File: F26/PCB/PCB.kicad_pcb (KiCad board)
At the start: 2 copper layers, 6 parts, among them J3 B2B-XH-A, J4 B3B-XH-A, U4 815, U6 SC0194_9_

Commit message: Unfinished PCB Design
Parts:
- added SW1: SW_Nidec_CAS-120A1, Button_Switch_SMD:Nidec_Copal_CAS-120A, F.Cu at (73.5, 97.8)
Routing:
- net Net-(U1-A5): track 108.3 -> 166.6 mm
- net Net-(U4-~{OE}-PadOE_1): track 0.00 -> 58.3 mm
- net Net-(U1-A4): track 71.9 -> 130.2 mm
- net Net-(SW1-B): track 129.0 -> 180.4 mm

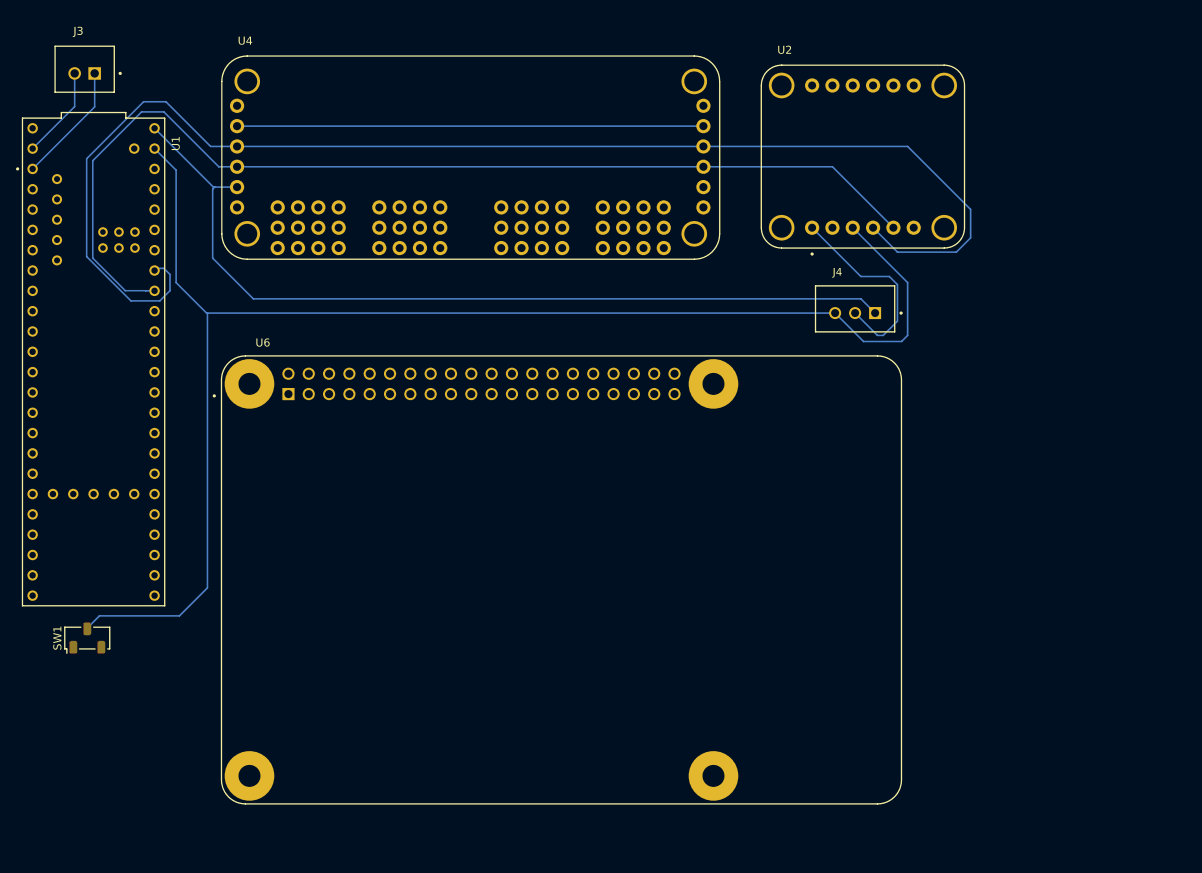
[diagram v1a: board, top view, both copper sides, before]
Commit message: Worded on PCB and teensy implementation
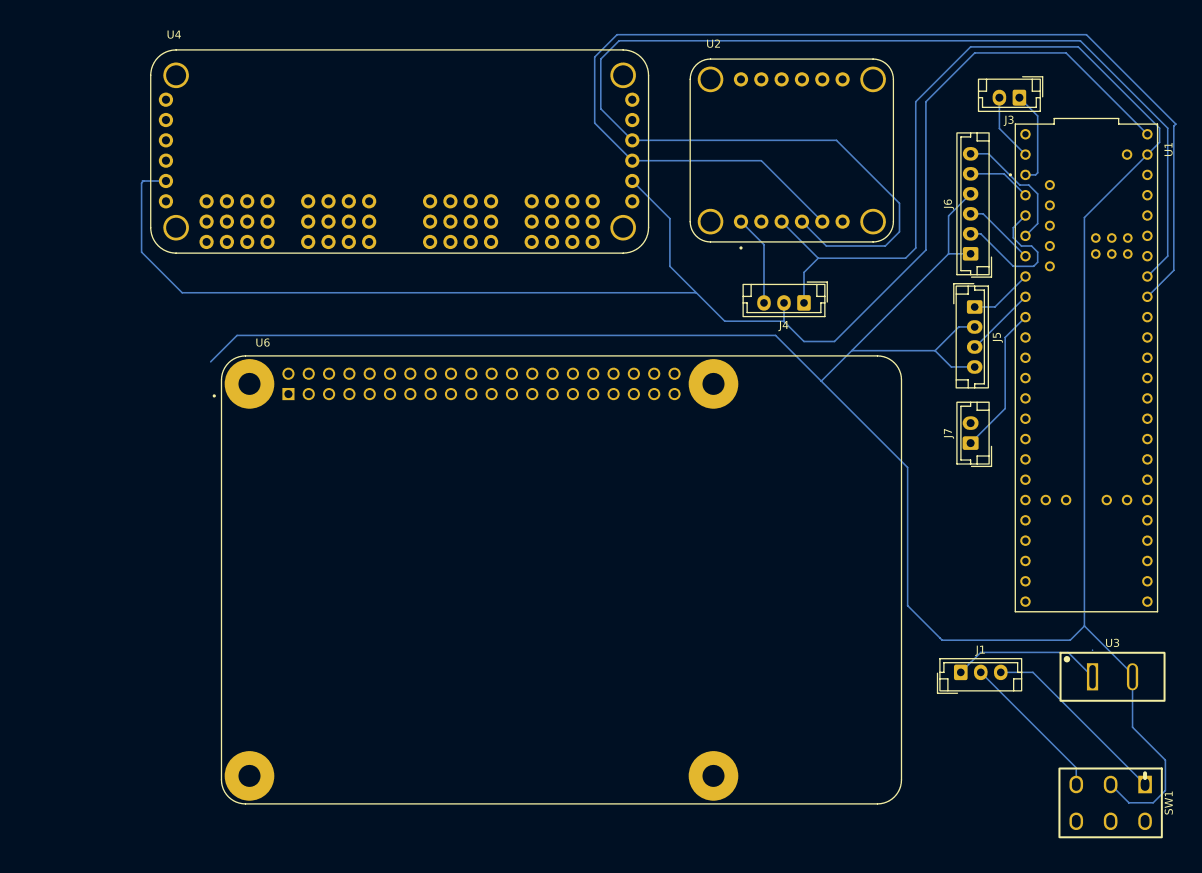
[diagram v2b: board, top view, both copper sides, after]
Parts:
- added J1: B3B-XH-A, Connector_JST:JST_EH_B3B-EH-A_1x03_P2.50mm_Vertical, F.Cu at (182.7, 102.1)
- added J5: Conn_01x04, Connector_JST:JST_EH_B4B-EH-A_1x04_P2.50mm_Vertical, F.Cu at (184.4, 56.4)
- added J6: Conn_01x06, Connector_JST:JST_EH_B6B-EH-A_1x06_P2.50mm_Vertical, F.Cu at (183.9, 49.7)
- added J7: Conn_01x02, Connector_JST:JST_EH_B2B-EH-A_1x02_P2.50mm_Vertical, F.Cu at (183.9, 73.4)
- added U3: ~, Button:Switch_2Pin_5mm_ParallelBlades, F.Cu at (199.1, 102.6)
- J3: footprint JST:JST -> Connector_JST:JST_EH_B2B-EH-A_1x02_P2.50mm_Vertical
- J4: footprint JST3:JST3 -> Connector_JST:JST_EH_B3B-EH-A_1x03_P2.50mm_Vertical
- SW1: footprint Button_Switch_SMD:Nidec_Copal_CAS-120A -> Switch:Mini_Toggle_DPDT_4.3x4.6mm
- moved SW1 129.6 mm to (201.4, 118.4), turned to -90 degrees
- moved U1 124.1 mm to (198.4, 64.0)
- moved J3 116.9 mm to (190.0, 30.2), turned to 180 degrees
- moved U4 8.92 mm to (112.5, 37.0)
- moved U2 8.92 mm to (161.5, 36.8)
- moved J4 6.43 mm to (163.1, 55.9), turned to 180 degrees
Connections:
- J4 pad 1: VCC -> Net-(J5-Pin_2)
- J4 pad 2: Net-(U2-VIN) -> VCC
- J4 pad 3: Net-(SW1-B) -> Net-(U2-VIN)
- SW1 pad 2: Net-(SW1-B) -> Net-(J5-Pin_2)
- U1 pad 2: unconnected-(U1-OUT2-Pad2) -> Net-(J6-Pin_5)
- U1 pad 3: unconnected-(U1-LRCLK2-Pad3) -> Net-(J6-Pin_2)
- U1 pad 4: unconnected-(U1-BCLK2-Pad4) -> Net-(J6-Pin_6)
- U1 pad 5: unconnected-(U1-IN2-Pad5) -> Net-(J6-Pin_3)
- U1 pad 6: unconnected-(U1-OUT1D-Pad6) -> Net-(J5-Pin_1)
- U1 pad 7: unconnected-(U1-OUT1A-Pad7) -> Net-(J5-Pin_3)
- U1 pad 8: unconnected-(U1-IN1-Pad8) -> Net-(J7-Pin_1)
- U1 pad GND: Net-(SW1-B) -> Net-(J5-Pin_2)
- U2 pad 3: Net-(SW1-B) -> Net-(J5-Pin_2)
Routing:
- net Net-(J5-Pin_2): track 0.00 -> 374.2 mm
- net Net-(SW1-B): track 180.4 -> 0.00 mm
- net VCC: track 108.0 -> 191.9 mm
- net Net-(U4-~{OE}-PadOE_1): track 58.3 -> 0.00 mm
- net Net-(SW1-C): track 0.00 -> 23.8 mm
- net Net-(SW1-A): track 0.00 -> 19.0 mm
- net Net-(J1-Pad1): track 0.00 -> 18.8 mm
- net Net-(J6-Pin_2): track 0.00 -> 18.8 mm
- net Net-(J7-Pin_1): track 0.00 -> 18.6 mm
- net Net-(J6-Pin_6): track 0.00 -> 16.3 mm
- net Net-(U2-VIN): track 25.4 -> 11.9 mm
- net Net-(U1-A4): track 130.2 -> 143.3 mm
- net Net-(J6-Pin_3): track 0.00 -> 9.05 mm
- net Net-(J5-Pin_3): track 0.00 -> 8.95 mm
- net Net-(J6-Pin_5): track 0.00 -> 7.96 mm
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
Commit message: PCB updates and Made wiring diagram
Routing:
- net Net-(J5-Pin_2): track 374.2 -> 294.1 mm
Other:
- board outline added: 134.4 x 105.1 mm

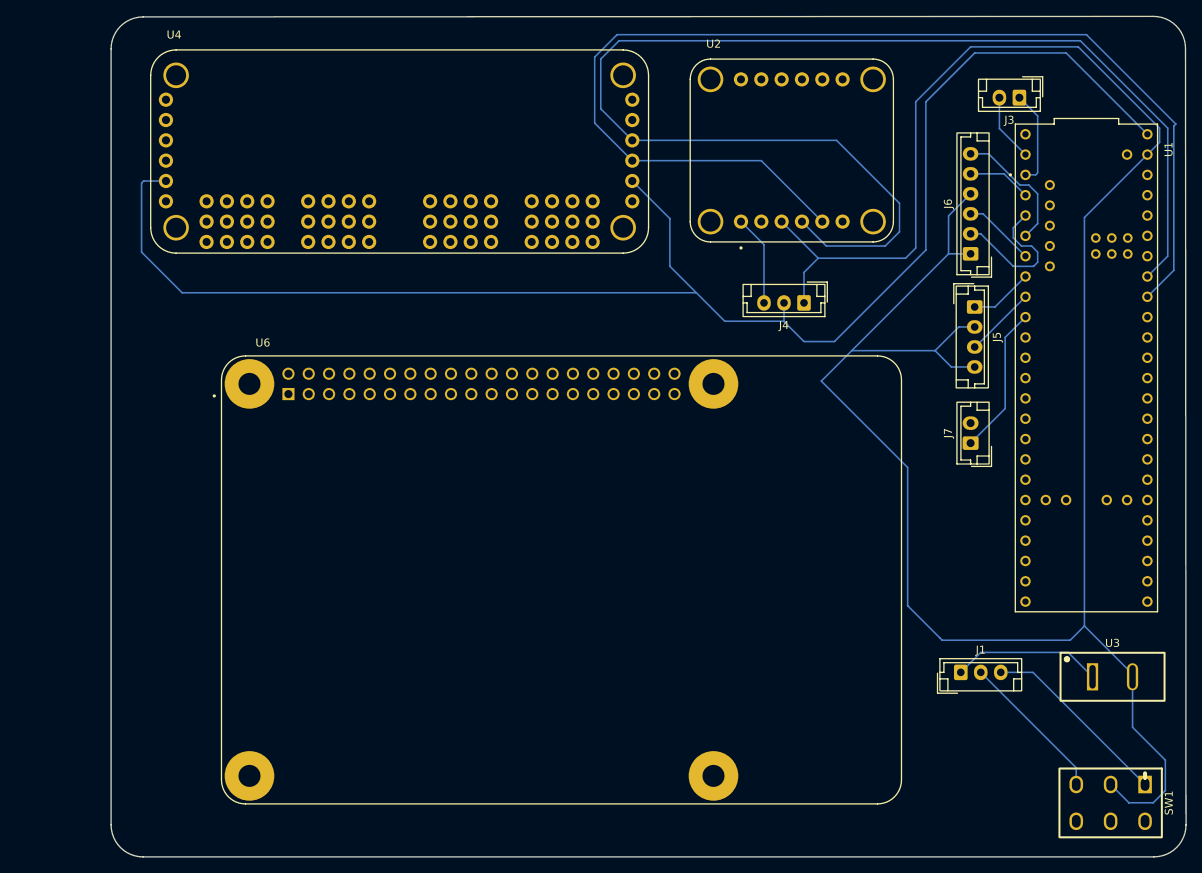
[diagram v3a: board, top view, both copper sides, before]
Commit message: Revert "PCB updates and Made wiring diagram"
This reverts commit 1d9744c909245b32a5317365d398eff2a277c9bc.
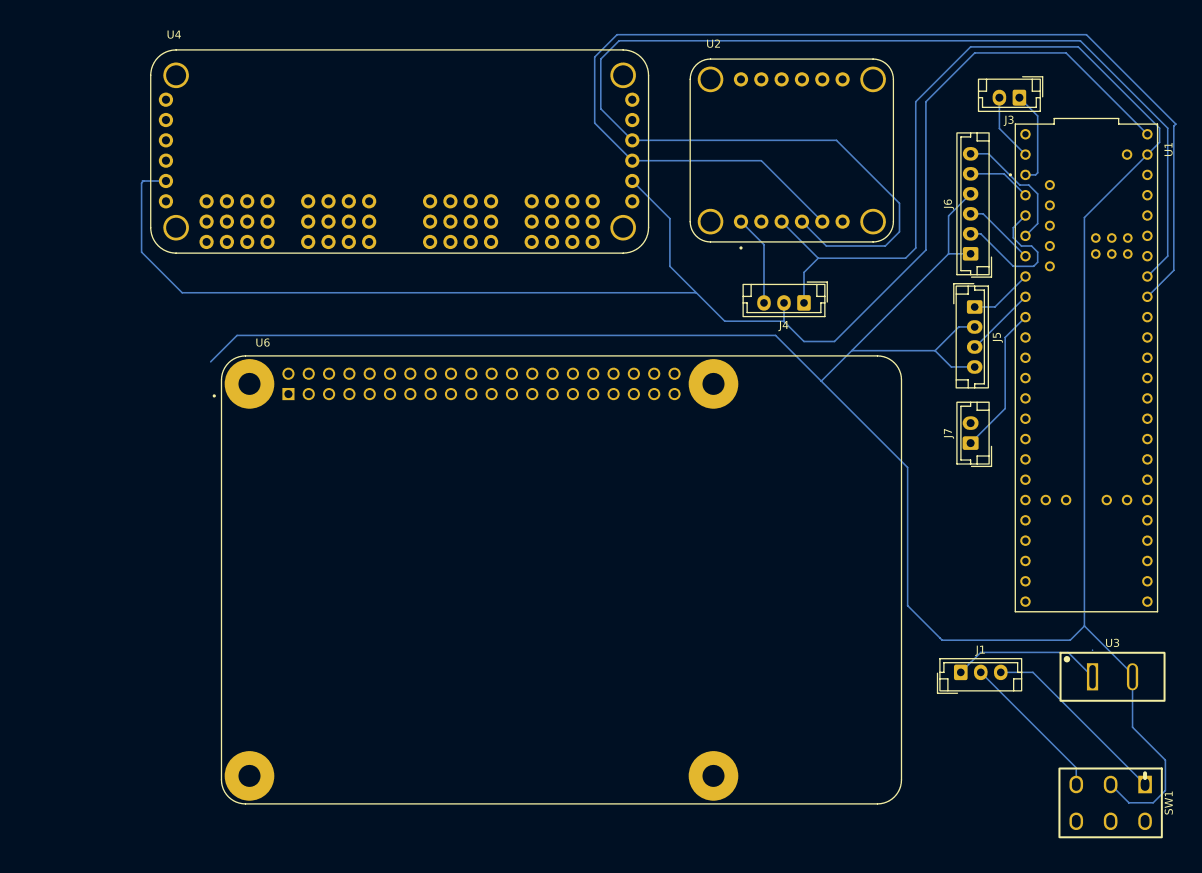
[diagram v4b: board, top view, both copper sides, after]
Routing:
- net Net-(J5-Pin_2): track 294.1 -> 374.2 mm
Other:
- board outline removed
